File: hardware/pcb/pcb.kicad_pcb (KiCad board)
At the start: 2 copper layers, 92 parts, among them J1 PRT-12639, K1 KEYSW, K10 KEYSW, K11 KEYSW, K12 KEYSW, K13 KEYSW, K14 KEYSW, K15 KEYSW, K16 KEYSW, K17 KEYSW, K18 KEYSW, K19 KEYSW, K2 KEYSW, K20 KEYSW, K21 KEYSW, K22 KEYSW, K23 KEYSW, K24 KEYSW, K25 KEYSW, K26 KEYSW, K27 KEYSW, K28 KEYSW, K29 KEYSW, K3 KEYSW, K30 KEYSW, K31 KEYSW, K32 KEYSW, K33 KEYSW, K34 KEYSW, K35 KEYSW, K36 KEYSW, K37 KEYSW, K38 KEYSW, K39 KEYSW, K4 KEYSW, K40 KEYSW, K41 KEYSW, K42 KEYSW, K43 KEYSW, K44 KEYSW, K5 KEYSW, K6 KEYSW, K7 KEYSW, K8 KEYSW, K9 KEYSW, U1 RP2040_Zero

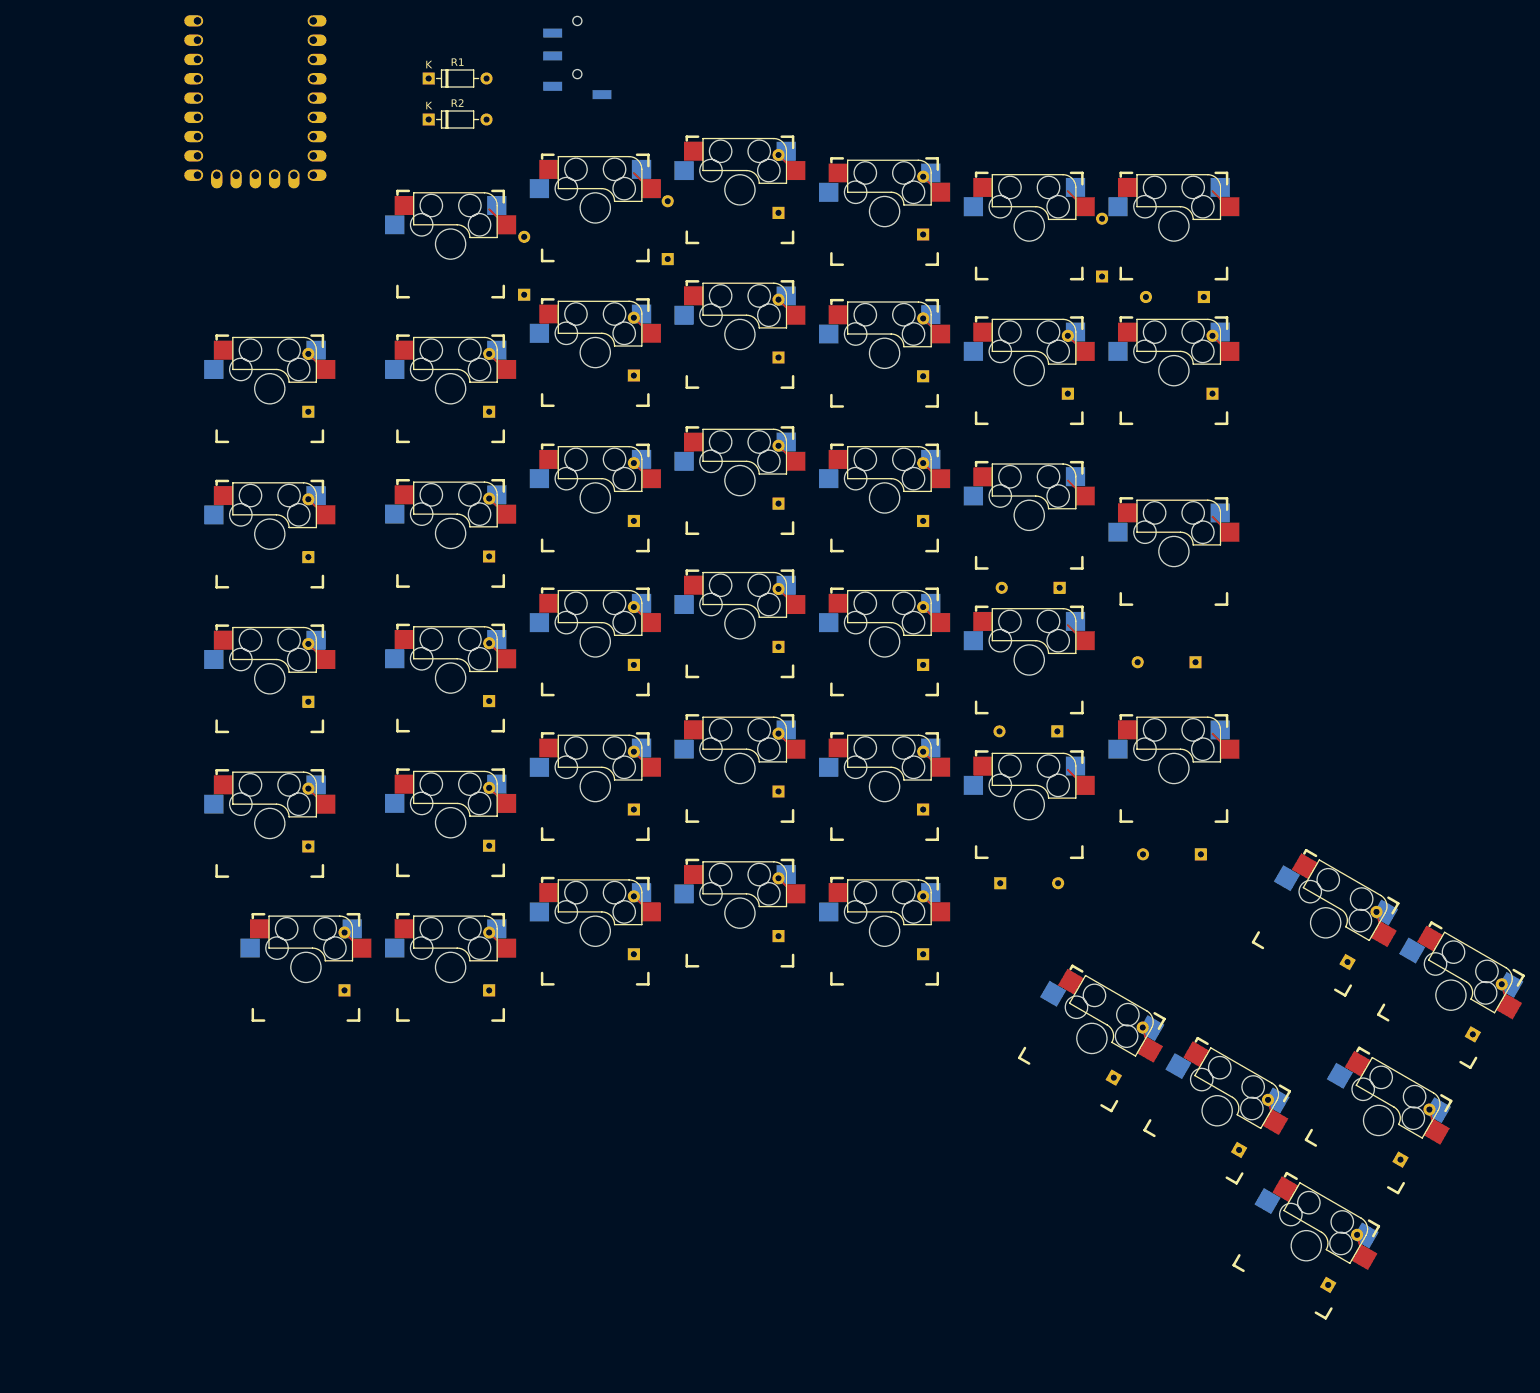
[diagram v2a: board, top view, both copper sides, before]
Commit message: placed switched to ergomax layout using plugin, and added edge cuts for castelled rp2040 zero
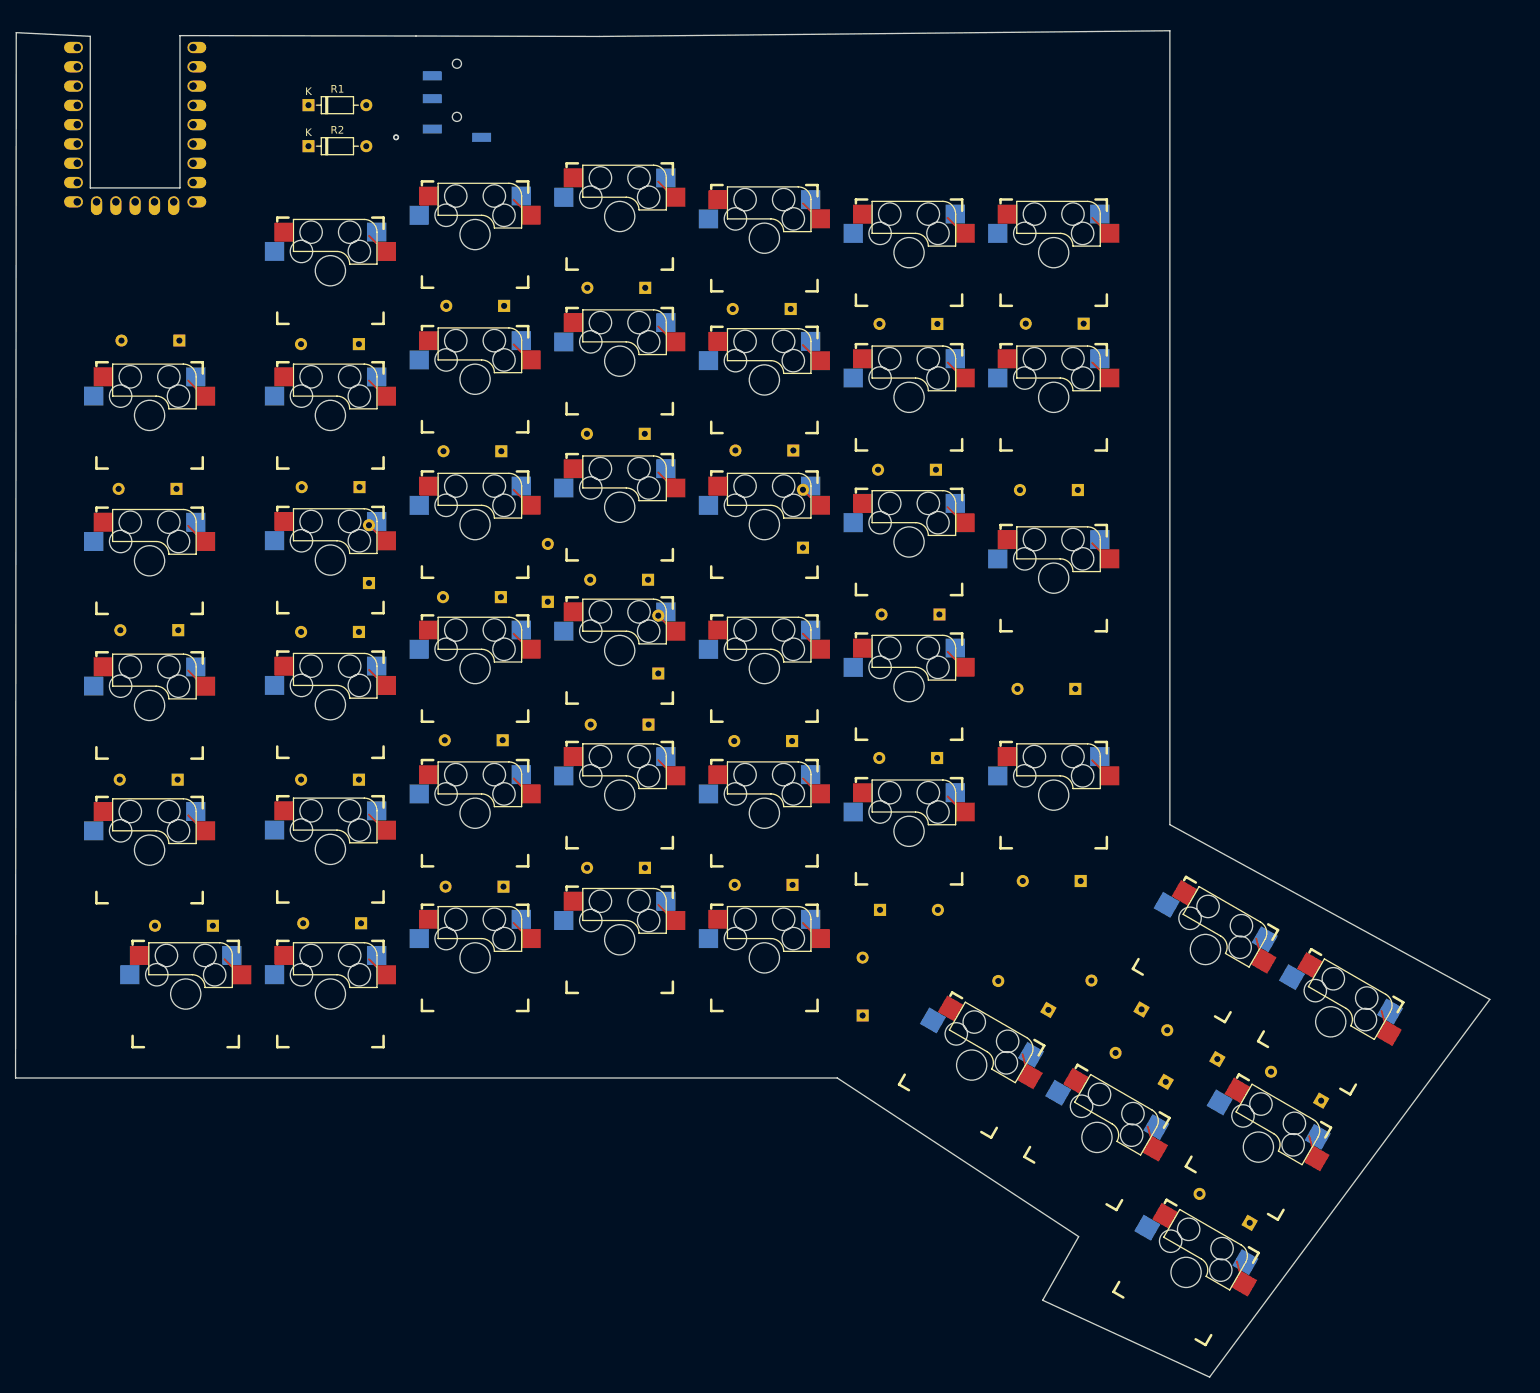
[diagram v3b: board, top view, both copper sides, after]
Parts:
- moved D40 33.8 mm to (199.6, 158.2), turned to 150 degrees
- moved D39 27.8 mm to (189.6, 151.6), turned to 150 degrees
- moved D6 22.7 mm to (86.5, 64.0), turned to 180 degrees
- moved D4 22.6 mm to (162.7, 61.4), turned to 180 degrees
- moved D2 22.4 mm to (105.7, 59.0), turned to 180 degrees
- moved D11 21.8 mm to (181.2, 83.2), turned to 180 degrees
- moved D7 20.3 mm to (124.2, 75.8), turned to 180 degrees
- moved D1 20.1 mm to (124.2, 56.6), turned to 180 degrees
- moved D8 20.1 mm to (105.3, 78.1), turned to 180 degrees
- moved D10 20.1 mm to (162.5, 80.5), turned to 180 degrees
- moved D3 20.0 mm to (143.4, 59.4), turned to 180 degrees
- moved D23 20.0 mm to (143.6, 116.3), turned to 180 degrees
- moved D14 19.9 mm to (124.6, 95.0), turned to 180 degrees
- moved D30 19.9 mm to (143.6, 135.2), turned to 180 degrees
- moved D34 19.8 mm to (124.2, 133.0), turned to 180 degrees
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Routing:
- net (no net): vias 0 -> 1
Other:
- board outline added: 194.2 x 177.3 mm

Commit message: routing
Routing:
- net R5: track 0.00 -> 419.1 mm, vias 0 -> 5
- net R4: track 0.00 -> 409.5 mm, vias 0 -> 5
- net R1: track 0.00 -> 360.4 mm, vias 0 -> 2
- net C4: track 0.00 -> 337.8 mm
- net C3: track 0.00 -> 333.6 mm, vias 0 -> 2
- net R3: track 0.00 -> 313.8 mm, vias 0 -> 11
- net R0: track 0.00 -> 278.7 mm
- net C5: track 0.00 -> 270.3 mm, vias 0 -> 2
- net C6: track 0.00 -> 263.6 mm
- net C2: track 0.00 -> 259.1 mm
- net C1: track 0.00 -> 244.9 mm, vias 0 -> 2
- net C0: track 0.00 -> 241.5 mm
- net R2: track 0.00 -> 226.8 mm, vias 0 -> 6
- net C7: track 0.00 -> 122.0 mm
- net SCL: track 0.00 -> 58.3 mm
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
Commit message: removed outline, to add rj45
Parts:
- added REF**: robu45vb_1, vbdox:robu45vb_1, F.Cu at (161.2, 31.6)
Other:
- board size 194.2 x 177.3 mm -> 384.6 x 257.5 mm
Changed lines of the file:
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@@
     )
   )
+  (footprint "vbdox:robu45vb_1" (layer "F.Cu")
+    (at 161.175 31.63)
+    (attr through_hole)
+    (fp_text reference "REF**" (at 0 -0.5 unlocked) (layer "F.SilkS") hide
+        (effects (font (size 1 1) (thickness 0.1)))
+    )
+    (fp_text value "robu45vb_1" (at 0 1 unlocked) (layer "F.Fab") hide
+        (effects (font (size 1 1) (thickness 0.15)))
+    )
+    (fp_rect (start 13.715 10.15) (end -2.285 -8.25)
+      (stroke (width 0.1) (type default)) (fill none) (layer "F.SilkS"))
+    (fp_circle (center 0 0) (end 1.45 0)
+      (stroke (width 0.05) (type default)) (fill none) (layer "Edge.Cuts"))
+    (fp_circle (center 11.43 0) (end 12.88 0)
+      (stroke (width 0.05) (type default)) (fill none) (layer "Edge.Cuts"))
+    (pad "1" thru_hole circle (at 6.35 8.89) (size 1.5 1.5) (drill 0.9) (layers "*.Cu" "*.Mask"))
+    (pad "2" thru_hole circle (at 5.08 6.35) (size 1.5 1.5) (drill 0.9) (layers "*.Cu" "*.Mask"))
+    (pad "3" thru_hole circle (at 7.62 6.35) (size 1.5 1.5) (drill 0.9) (layers "*.Cu" "*.Mask"))
+    (pad "4" thru_hole circle (at 10.16 6.35) (size 1.5 1.5) (drill 0.9) (layers "*.Cu" "*.Mask"))
+    (pad "6" thru_hole circle (at 2.54 6.35) (size 1.5 1.5) (drill 0.9) (layers "*.Cu" "*.Mask"))
+    (pad "8" thru_hole circle (at 8.89 8.89) (size 1.5 1.5) (drill 0.9) (layers "*.Cu" "*.Mask"))
+    (pad "10" thru_hole oval (at 13.715 -3.65) (size 0.6 2) (drill oval 0.3 1) (layers "*.Cu" "*.Mask"))
+    (pad "11" thru_hole circle (at 3.81 8.89) (size 1.5 1.5) (drill 0.9) (layers "*.Cu" "*.Mask"))
+    (pad "12" thru_hole circle (at 1.27 8.89) (size 1.5 1.5) (drill 0.9) (layers "*.Cu" "*.Mask"))
+    (pad "14" thru_hole oval (at -2.285 -3.65) (size 0.6 2) (drill oval 0.3 1) (layers "*.Cu" "*.Mask"))
+  )
   (footprint "vbdox:Kailh_MX_Socket_reversible" (layer "F.Cu")
     (at 178.03 51.9625)
@@
     )
   )
-  (gr_line (start 193.33 127.29) (end 235.47 150.3)
-    (stroke (width 0.1) (type default)) (layer "Edge.Cuts"))
-  (gr_line (start 198.56 200.04) (end 176.58 189.92)
-    (stroke (width 0.1) (type default)) (layer "Edge.Cuts"))
-  (gr_line (start 118.21 23.49) (end 193.33 22.74)
-    (stroke (width 0.1) (type default)) (layer "Edge.Cuts"))
-  (gr_line (start 51.16 43.44) (end 62.97 43.44)
-    (stroke (width 0.1) (type default)) (layer "Edge.Cuts"))
-  (gr_line (start 176.58 189.92) (end 181.32 181.54)
-    (stroke (width 0.1) (type default)) (layer "Edge.Cuts"))
-  (gr_line (start 235.47 150.3) (end 198.56 200.04)
-    (stroke (width 0.1) (type default)) (layer "Edge.Cuts"))
-  (gr_line (start 41.32 160.65) (end 41.41 22.99)
-    (stroke (width 0.1) (type default)) (layer "Edge.Cuts"))
-  (gr_line (start 62.97 23.38) (end 94.05 23.43)
-    (stroke (width 0.1) (type default)) (layer "Edge.Cuts"))
-  (gr_line (start 181.32 181.54) (end 149.53 160.65)
-    (stroke (width 0.1) (type default)) (layer "Edge.Cuts"))
-  (gr_line (start 193.33 22.74) (end 193.33 127.29)
-    (stroke (width 0.1) (type default)) (layer "Edge.Cuts"))
-  (gr_line (start 94.05 23.43) (end 118.21 23.49)
-    (stroke (width 0.1) (type default)) (layer "Edge.Cuts"))
-  (gr_line (start 62.97 43.44) (end 62.97 23.38)
-    (stroke (width 0.1) (type default)) (layer "Edge.Cuts"))
-  (gr_line (start 51.16 23.47) (end 41.41 22.99)
-    (stroke (width 0.1) (type default)) (layer "Edge.Cuts"))
-  (gr_line (start 51.16 23.47) (end 51.16 43.44)
-    (stroke (width 0.1) (type default)) (layer "Edge.Cuts"))
-  (gr_line (start 149.53 160.65) (end 41.32 160.65)
-    (stroke (width 0.1) (type default)) (layer "Edge.Cuts"))
+  (gr_rect (start -61.78 -30.99) (end 322.84 226.51)
+    (stroke (width 0.1) (type default)) (fill none) (layer "Edge.Cuts"))
   (segment (start 85.1178 117.297) (end 103.206 117.297) (width 0.25) (layer "F.Cu") (net 1))
   (segment (start 54.8637 44.0203) (end 55.8 44.9566) (width 0.25) (layer "F.Cu") (net 1))

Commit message: prod
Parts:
- added ?: GND, ScottoKeebs_Components:Diode_DO-35, B.Cu at (154.1, 36.3)
- added ?: GND, ScottoKeebs_Components:Diode_DO-35, B.Cu at (154.1, 31.3)
- added ?: GND, ScottoKeebs_Components:Diode_DO-35, B.Cu at (154.1, 28.8)
- added ?: GND, ScottoKeebs_Components:Diode_DO-35, B.Cu at (154.1, 33.8)
- added G***: LOGO, logo:VBincLogo, F.Cu at (86.9, 132.1)
- added G***: LOGO, logo:VBincLogo, B.Cu at (88.9, 132.6)
- REF**: moved to B.Cu
- moved REF** 13.3 mm to (174.4, 31.6), turned to 180 degrees
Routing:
- net (no net): track 0.00 -> 75.9 mm
- net SDA: track 51.4 -> 51.5 mm, vias 0 -> 1
- net SCL: track 58.3 -> 58.4 mm, vias 0 -> 1
- net VCC: vias 0 -> 1
- net GND: track 41.8 -> 41.9 mm, vias 0 -> 1
- added copper zone on B.Cu, net (none)
- added copper zone on F.Cu, net (none)
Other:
- board size 384.6 x 257.5 mm -> 183.2 x 174.8 mm
- board text added: "VBdox"
- board text added: "udithvb.com/vbkeebs"
